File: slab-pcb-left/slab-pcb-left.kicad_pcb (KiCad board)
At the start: 2 copper layers, 158 x 104 mm, 127 parts, among them J1 MagnetR, J2 MagnetL, J3 TRRS_R, J4 TRRS_L, J5 SSD1306, J6 Conn_01x06, Q1 MMBT3906, SW1 RotaryEncoder, U1 Seeeduino Xiao rp2040, U2 PCA9555PW, U3 PCA9555PW, U4 ADS1110, U5 PW14

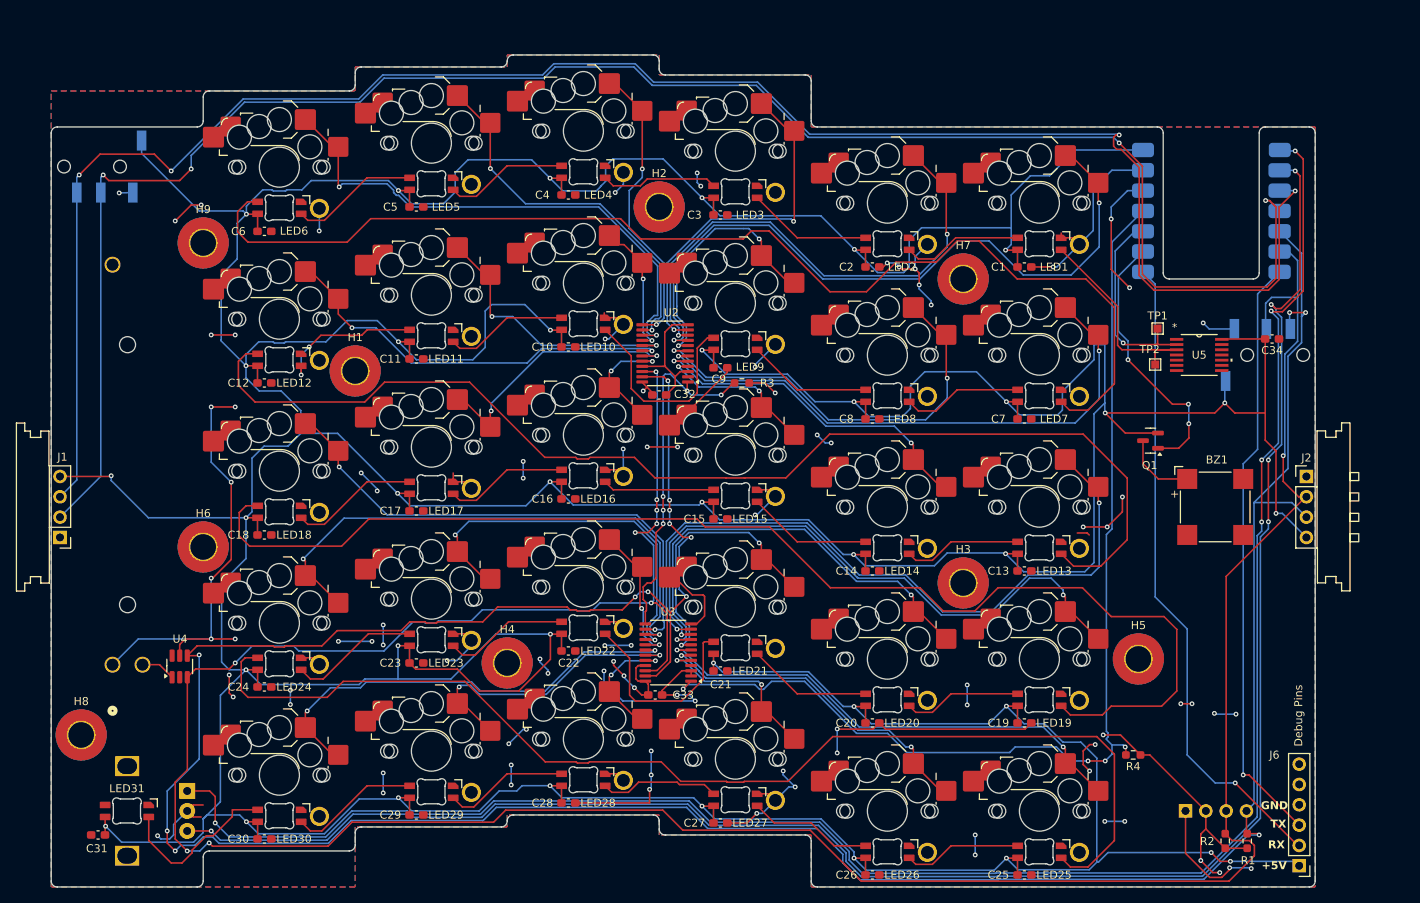
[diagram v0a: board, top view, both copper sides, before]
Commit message: fix: upside-down magnetic connectors
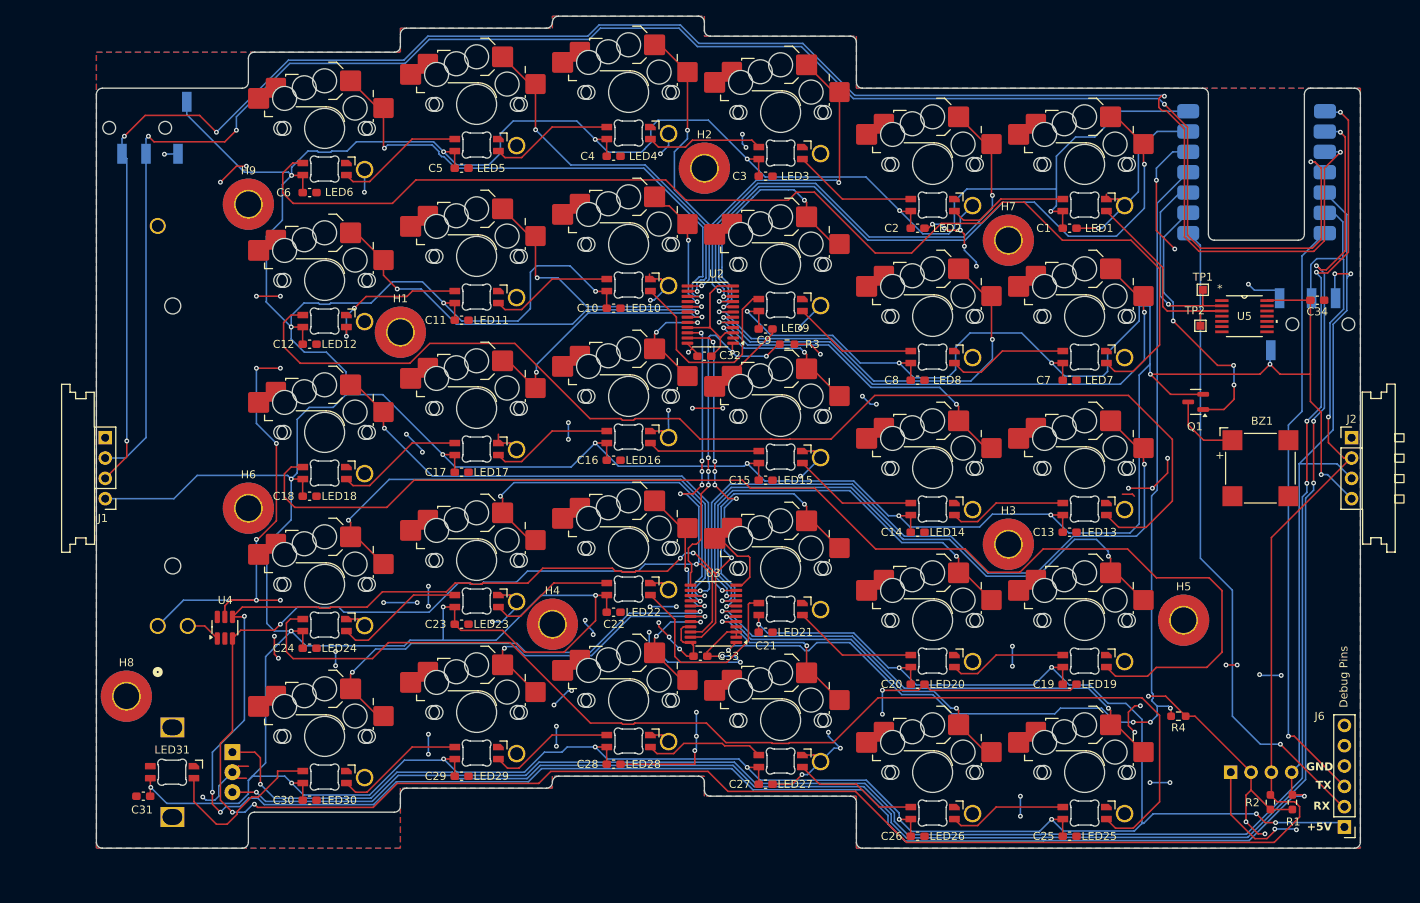
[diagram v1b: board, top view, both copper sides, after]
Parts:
- moved C6 7.44 mm to (98.7, 58.0)
- moved BZ1 7.44 mm to (217.5, 92.5)
- moved C1 7.44 mm to (193.7, 62.5)
- moved C10 7.44 mm to (136.7, 72.5)
- moved C11 7.44 mm to (117.7, 74.0)
- moved C12 7.44 mm to (98.7, 77.0)
- moved C13 7.44 mm to (193.7, 100.5)
- moved C14 7.44 mm to (174.7, 100.5)
- moved C15 7.44 mm to (155.7, 94.0)
- moved C16 7.44 mm to (136.7, 91.5)
- moved C17 7.44 mm to (117.7, 93.0)
- moved C18 7.44 mm to (98.7, 96.0)
- moved C19 7.44 mm to (193.7, 119.5)
- moved C2 7.44 mm to (174.7, 62.5)
- moved C20 7.44 mm to (174.7, 119.5)
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- renumbered REF** to OSHW, REF** to WEEE
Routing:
- net /I2C0_SDA: track 235.0 -> 238.0 mm, vias 4 -> 5
- net VBUS: track 1012.5 -> 1011.3 mm, vias 37 -> 36
- net /I2C0_SCL: track 231.3 -> 230.3 mm

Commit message: fix: add voltage divider to potentiometer
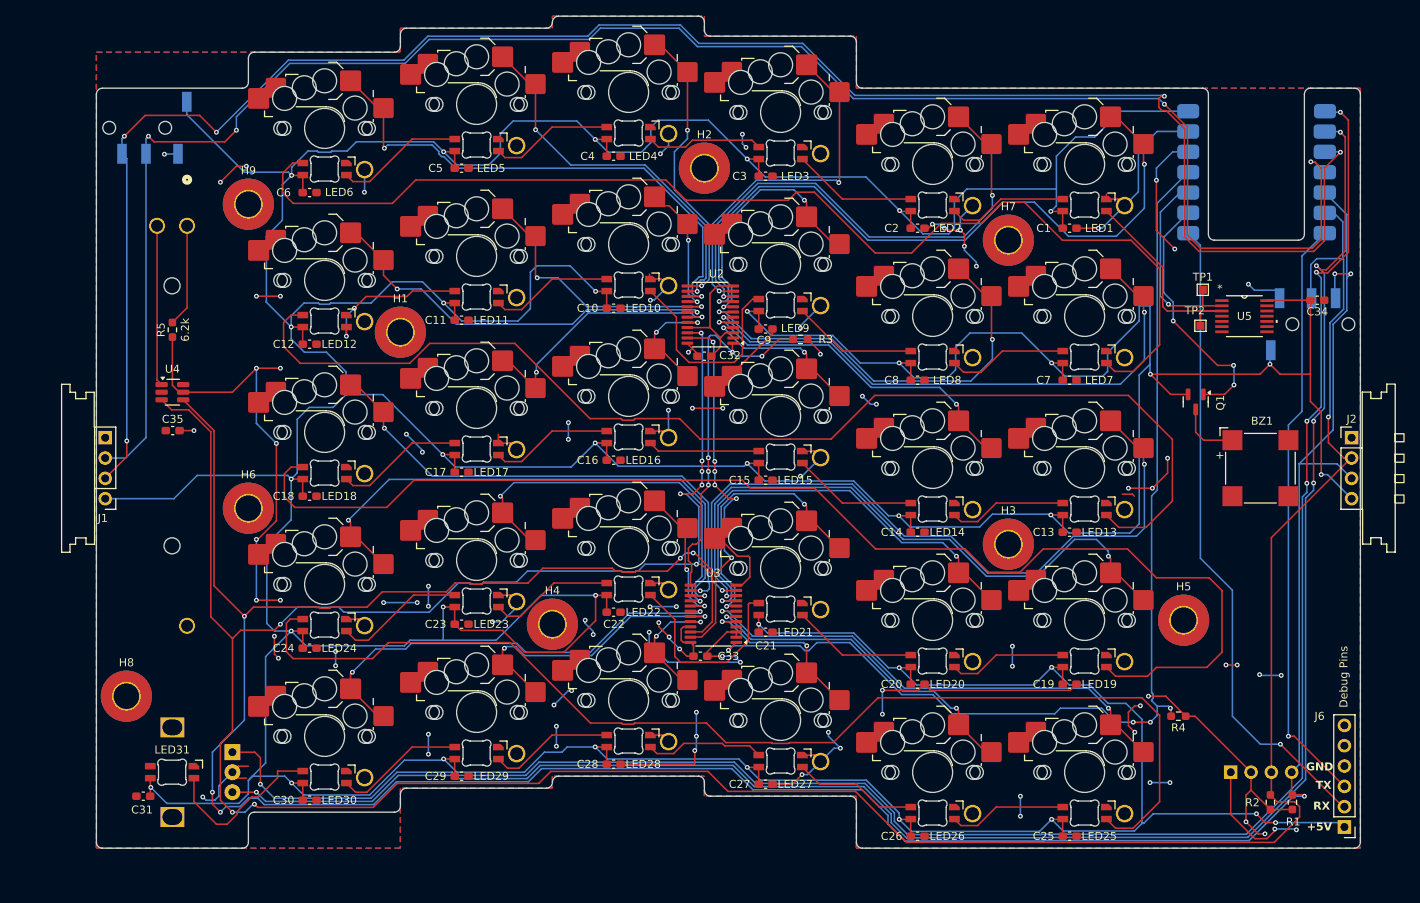
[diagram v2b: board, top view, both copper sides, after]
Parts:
- added C35: 100nF, Capacitor_SMD:C_0603_1608Metric_Pad1.08x0.95mm_HandSolder, F.Cu at (81.5, 87.8)
- added R5: 6.2k, Resistor_SMD:R_0603_1608Metric_Pad0.98x0.95mm_HandSolder, F.Cu at (81.5, 75.2)
- U5: value PW14 -> SN74AHCT125PWR
- moved RV1 50.2 mm to (83.3, 62.2), turned to -90 degrees
- moved U4 30.2 mm to (81.5, 83.0), turned to 0 degrees
- moved R3 1.77 mm to (160.0, 76.4)
- turned Q1 to -90 degrees
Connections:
- RV1 pad 1: +3V3 -> Net-(R5-Pad2)
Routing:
- net /I2C1_SCL: track 367.0 -> 401.8 mm
- net /I2C1_SDA: track 378.3 -> 405.4 mm
- net Net-(U4-VIN+): track 4.35 -> 20.1 mm
- net Net-(R5-Pad2): track 0.00 -> 12.8 mm
- net /EXPANDER1_INT: track 44.6 -> 46.5 mm
- net VBUS: track 1011.3 -> 1009.5 mm
- net /BUZZER: track 33.8 -> 31.9 mm
- net Net-(BZ1-+): track 9.18 -> 7.86 mm
- net +3V3: track 151.1 -> 150.5 mm, vias 31 -> 32
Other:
- board text added: "version 3.1 'nowhere'"
- board text removed: "version 3.0 'nowhere'"
